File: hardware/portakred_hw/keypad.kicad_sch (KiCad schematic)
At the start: 24 parts, among them SW1 SW_Push, SW10 SW_Push, SW11 SW_Push, SW12 SW_Push, SW2 SW_Push, SW3 SW_Push, SW4 SW_Push, SW5 SW_Push, SW6 SW_Push, SW7 SW_Push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

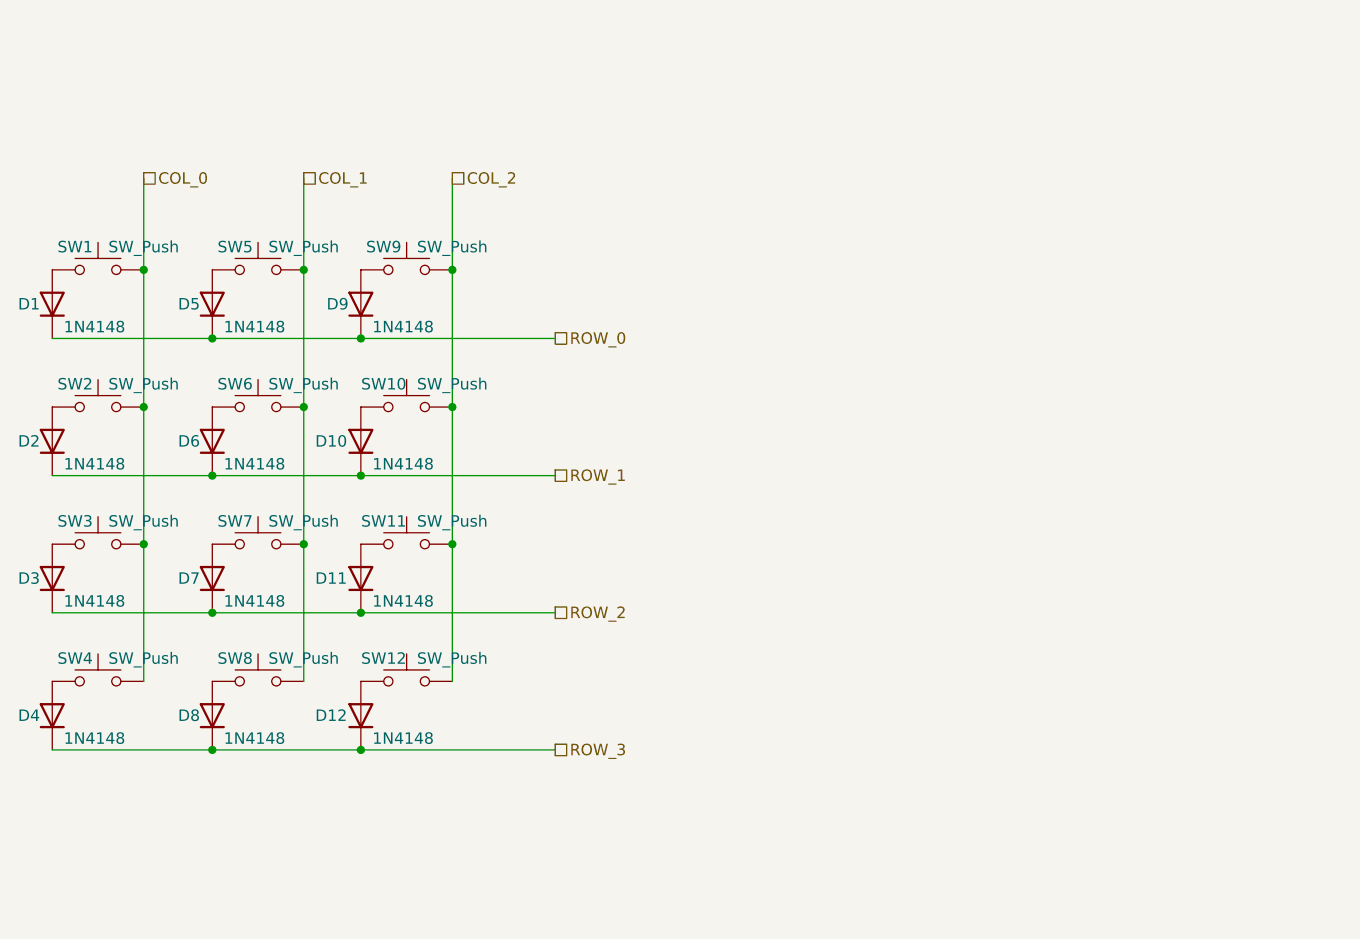
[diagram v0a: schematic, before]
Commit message: Fix buzzer connection, fix keypad diodes and add description, move NFC antenna wire to be pretty :)
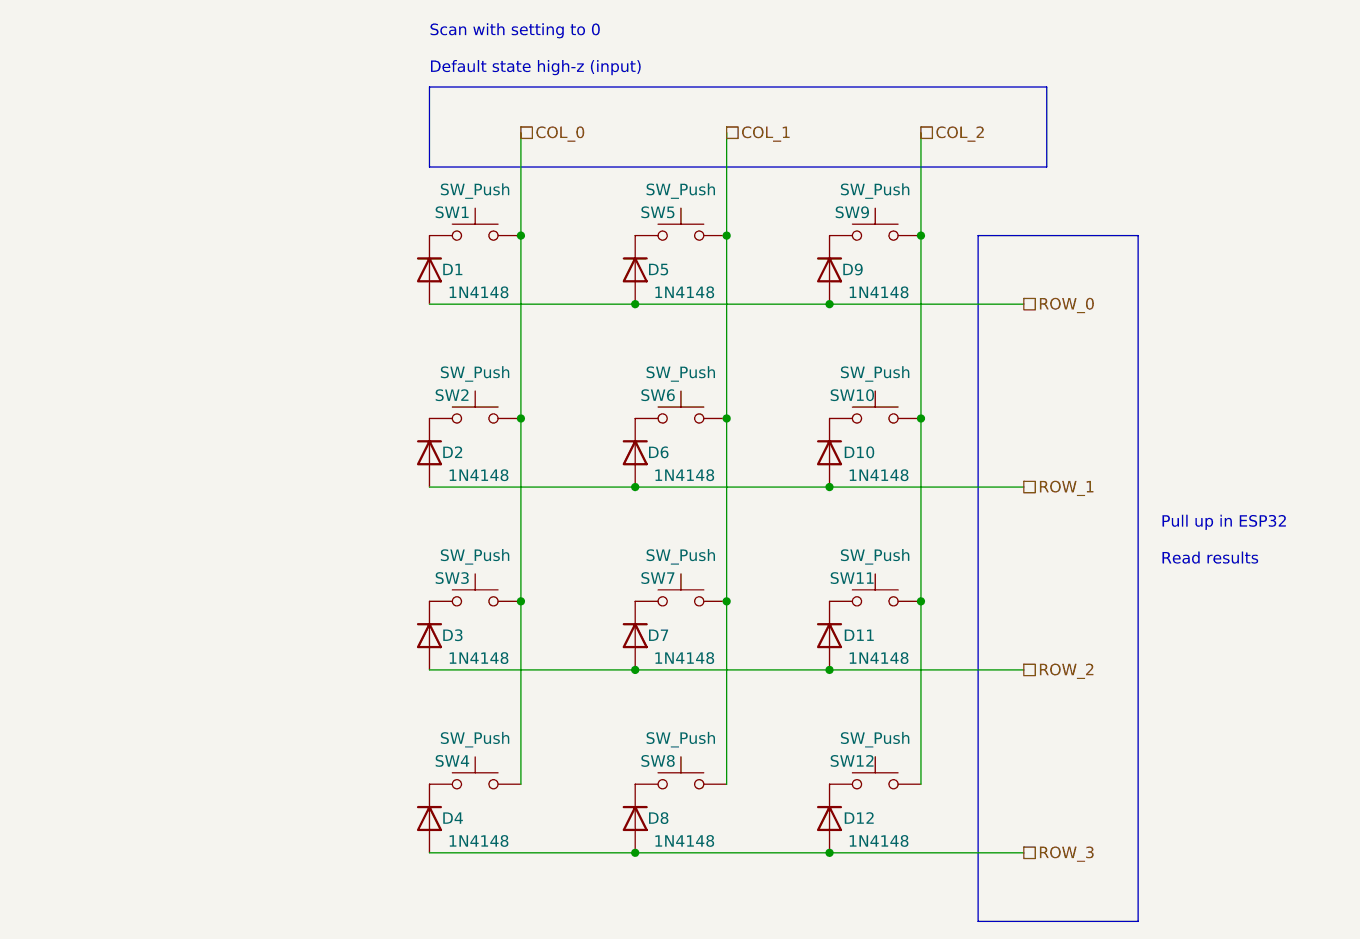
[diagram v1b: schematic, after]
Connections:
- net ROW_0: now also D1.2 (A), D5.2 (A), D9.2 (A); no longer D1.1 (K), D5.1 (K), D9.1 (K)
- net ROW_1: now also D10.2 (A), D2.2 (A), D6.2 (A); no longer D10.1 (K), D2.1 (K), D6.1 (K)
- net ROW_2: now also D11.2 (A), D3.2 (A), D7.2 (A); no longer D11.1 (K), D3.1 (K), D7.1 (K)
- net ROW_3: now also D12.2 (A), D4.2 (A), D8.2 (A); no longer D12.1 (K), D4.1 (K), D8.1 (K)
- net at SW12.1: now also D12.1 (K); no longer D12.2 (A)
- net at SW4.1: now also D4.1 (K); no longer D4.2 (A)
- net at SW10.1: now also D10.1 (K); no longer D10.2 (A)
- net at SW8.1: now also D8.1 (K); no longer D8.2 (A)
- net at SW1.1: now also D1.1 (K); no longer D1.2 (A)
- net at SW9.1: now also D9.1 (K); no longer D9.2 (A)
- net at SW3.1: now also D3.1 (K); no longer D3.2 (A)
- net at SW6.1: now also D6.1 (K); no longer D6.2 (A)
- net at SW2.1: now also D2.1 (K); no longer D2.2 (A)
- net at SW11.1: now also D11.1 (K); no longer D11.2 (A)
- net at SW7.1: now also D7.1 (K); no longer D7.2 (A)
- net at SW5.1: now also D5.1 (K); no longer D5.2 (A)
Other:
- note added: "Pull up in ESP32 Read results"
- note added: "Scan with setting to 0 Default state high-z (input)"
- moved on the sheet: D1, D10, D11, D12, D2, D3, D4, D5, D6, D7, D8, D9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
